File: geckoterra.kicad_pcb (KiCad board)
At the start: 2 copper layers, 50 x 50 mm, 21 parts, among them J1 Conn_WallSocket_Earth, J6 Conn_01x02, J7 Conn_01x02, J8 Conn_01x02, K1 SANYOU_SRD_Form_A, P1 Conn_WallPlug_Earth, Q1 2N3904, Q2 Q_NMOS_GDS, U1 PC817, U2 4N25

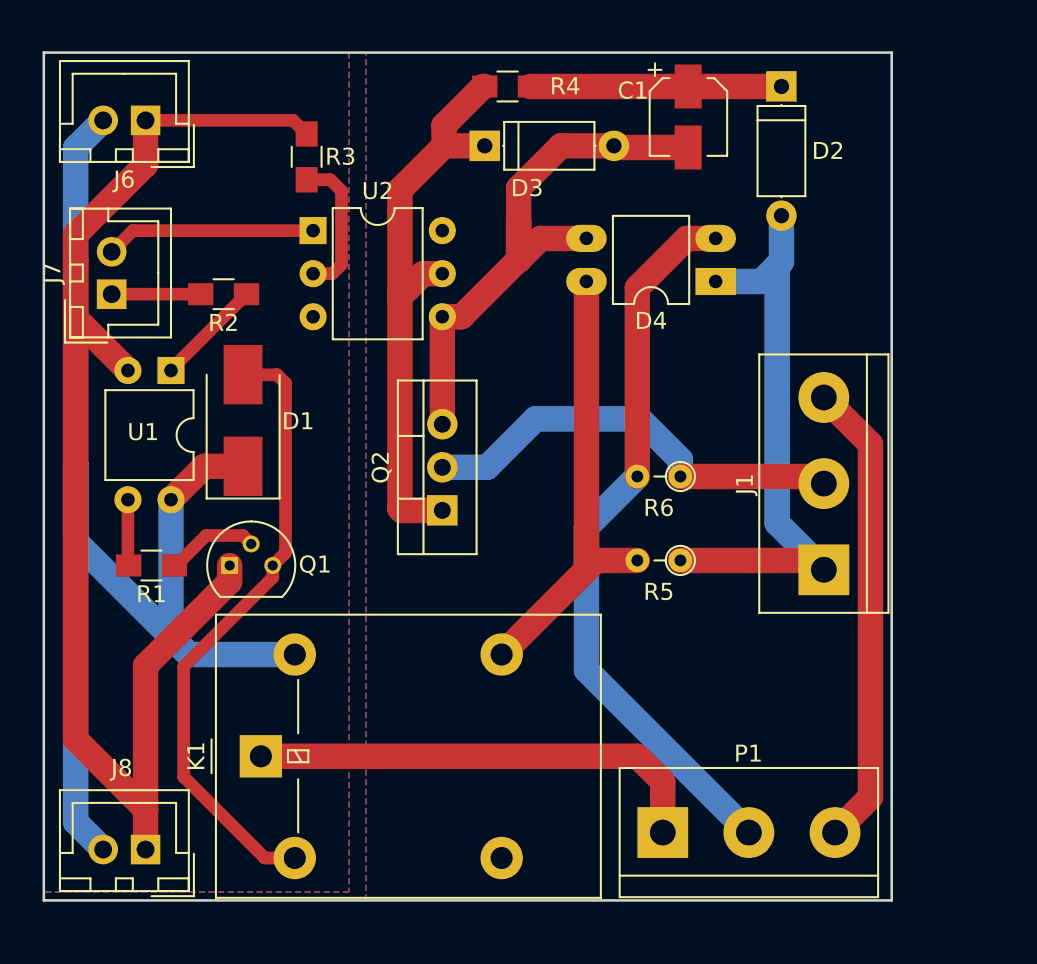
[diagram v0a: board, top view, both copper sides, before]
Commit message: Added screw holes
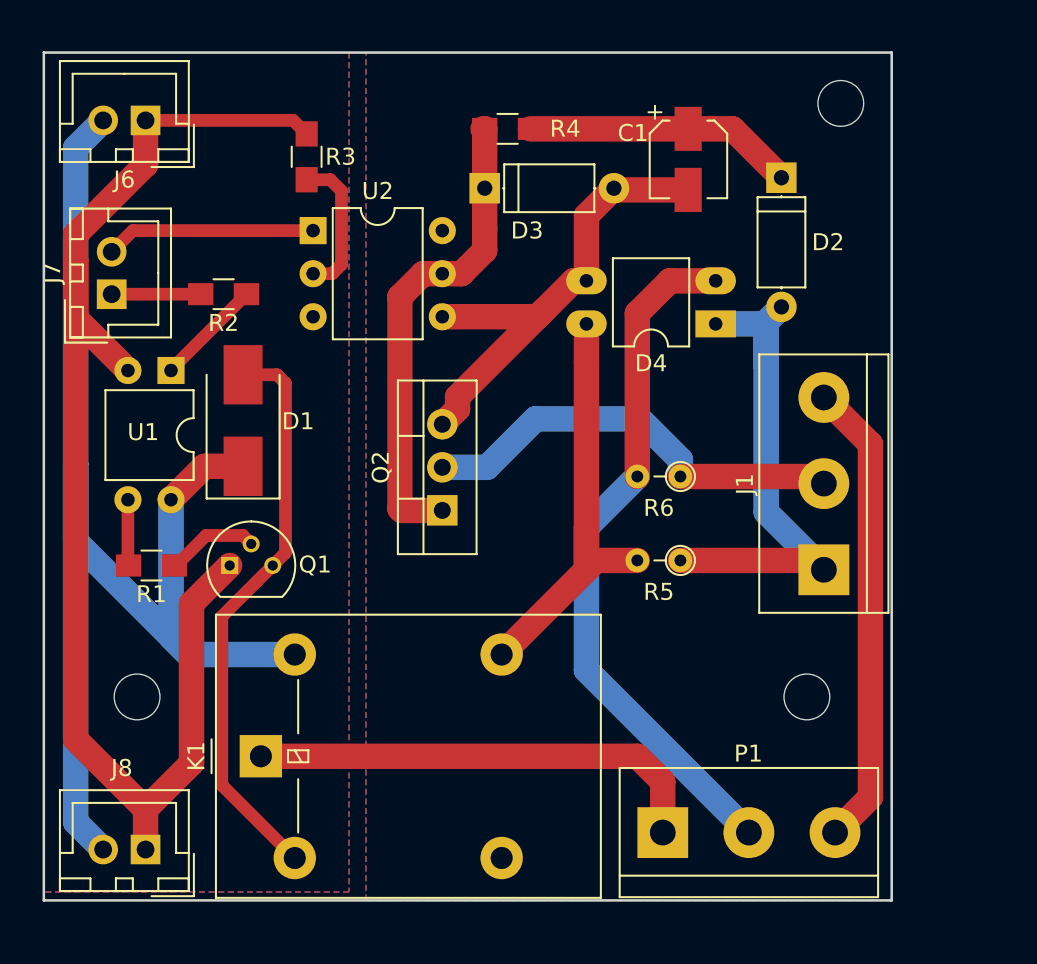
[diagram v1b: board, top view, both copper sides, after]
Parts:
- added SC1: MountingHole_2.7mm_M2.5, Mounting_Holes:MountingHole_2.7mm_M2.5, F.Cu at (55.5, 88.0)
- added SC1: MountingHole_2.7mm_M2.5, Mounting_Holes:MountingHole_2.7mm_M2.5, F.Cu at (97.0, 53.0)
- added SC2: MountingHole_2.7mm_M2.5, Mounting_Holes:MountingHole_2.7mm_M2.5, F.Cu at (95.0, 88.0)
- moved D2 5.38 mm to (93.5, 57.4)
- moved C1 2.50 mm to (88.0, 56.3)
- moved D3 2.50 mm to (76.0, 58.0)
- moved D4 2.50 mm to (89.6, 66.0)
- moved R4 2.50 mm to (77.3, 54.5)
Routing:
- net Net-(D3-Pad1): track 35.0 -> 28.4 mm
- net Net-(C1-Pad2): track 34.3 -> 29.1 mm
- net Net-(D2-Pad2): track 36.4 -> 32.5 mm
- net Net-(D1-Pad2): track 36.9 -> 34.0 mm
- net Net-(D4-Pad4): track 27.3 -> 24.8 mm
- net Net-(D4-Pad2): track 43.2 -> 41.2 mm
- net Net-(C1-Pad1): track 14.8 -> 16.0 mm

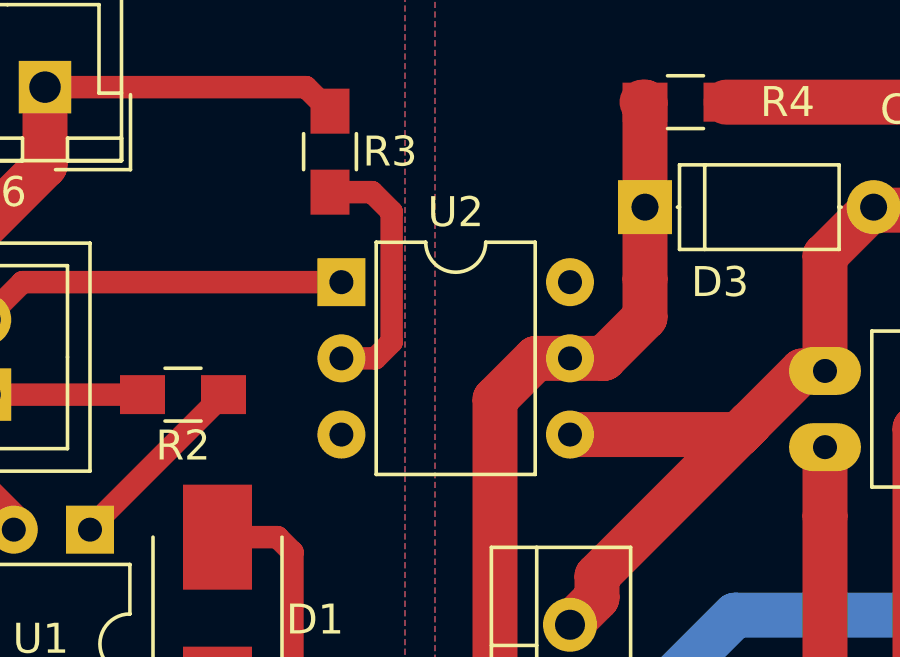
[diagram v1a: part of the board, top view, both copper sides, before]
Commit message: Add some references, change TH to SMD
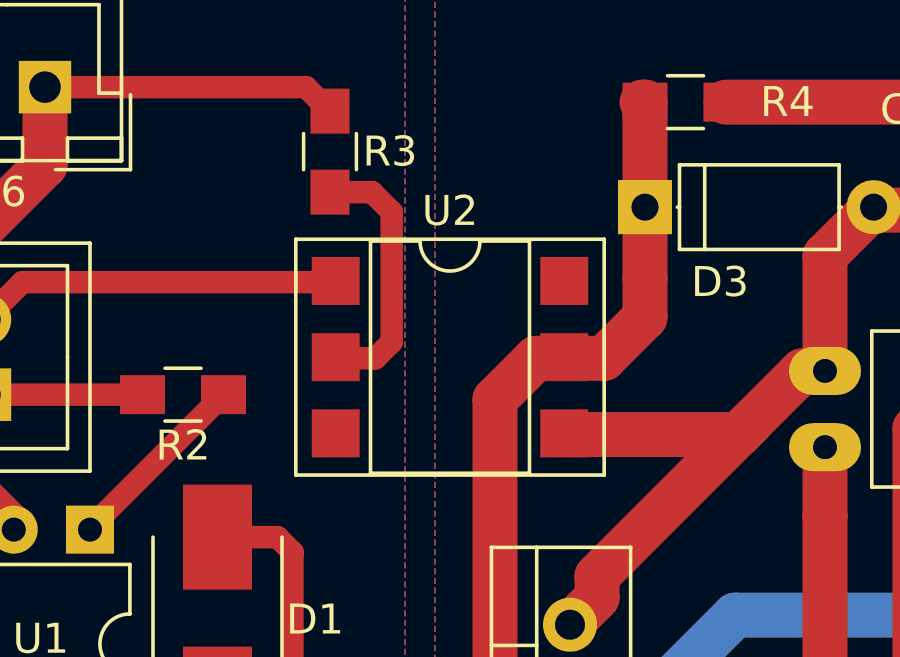
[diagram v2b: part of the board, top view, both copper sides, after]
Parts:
- U2: footprint Housings_DIP:DIP-6_W7.62mm -> Housings_DIP:DIP-6_W7.62mm_SMDSocket_SmallPads
- moved U2 4.40 mm to (69.5, 63.0)
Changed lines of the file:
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@@
-    )
-  )
-  (module Housings_DIP:DIP-6_W7.62mm (layer F.Cu)
-    (at 65.88 60.5)
-    (descr "6-lead though-hole mounted DIP package, row spacing 7.62 mm (300 mils)")
-    (tags "THT DIP DIL PDIP 2.54mm 7.62mm 300mil")
-    (fp_text reference U2 (at 3.81 -2.33) (layer F.SilkS)
-      (effects (font (size 1 1) (thickness 0.15)))
-    )
-    (fp_text value 4N25 (at 3.81 7.41) (layer F.Fab)
-      (effects (font (size 1 1) (thickness 0.15)))
-    )
-    (fp_arc (start 3.81 -1.33) (end 2.81 -1.33) (angle -180) (layer F.SilkS) (width 0.12))
-    (fp_line (start 1.635 -1.27) (end 6.985 -1.27) (layer F.Fab) (width 0.1))
-    (fp_line (start 6.985 -1.27) (end 6.985 6.35) (layer F.Fab) (width 0.1))
-    (fp_line (start 6.985 6.35) (end 0.635 6.35) (layer F.Fab) (width 0.1))
-    (fp_line (start 0.635 6.35) (end 0.635 -0.27) (layer F.Fab) (width 0.1))
-    (fp_line (start 0.635 -0.27) (end 1.635 -1.27) (layer F.Fab) (width 0.1))
-    (fp_line (start 2.81 -1.33) (end 1.16 -1.33) (layer F.SilkS) (width 0.12))
-    (fp_line (start 1.16 -1.33) (end 1.16 6.41) (layer F.SilkS) (width 0.12))
-    (fp_line (start 1.16 6.41) (end 6.46 6.41) (layer F.SilkS) (width 0.12))
-    (fp_line (start 6.46 6.41) (end 6.46 -1.33) (layer F.SilkS) (width 0.12))
-    (fp_line (start 6.46 -1.33) (end 4.81 -1.33) (layer F.SilkS) (width 0.12))
-    (fp_line (start -1.1 -1.55) (end -1.1 6.6) (layer F.CrtYd) (width 0.05))
-    (fp_line (start -1.1 6.6) (end 8.7 6.6) (layer F.CrtYd) (width 0.05))
-    (fp_line (start 8.7 6.6) (end 8.7 -1.55) (layer F.CrtYd) (width 0.05))
-    (fp_line (start 8.7 -1.55) (end -1.1 -1.55) (layer F.CrtYd) (width 0.05))
-    (fp_text user %R (at 3.81 2.54) (layer F.Fab)
-      (effects (font (size 1 1) (thickness 0.15)))
-    )
-    (pad 1 thru_hole rect (at 0 0) (size 1.6 1.6) (drill 0.8) (layers *.Cu *.Mask)
-      (net 13 /PWMPin))
-    (pad 4 thru_hole oval (at 7.62 5.08) (size 1.6 1.6) (drill 0.8) (layers *.Cu *.Mask)
-      (net 2 "Net-(C1-Pad2)"))
-    (pad 2 thru_hole oval (at 0 2.54) (size 1.6 1.6) (drill 0.8) (layers *.Cu *.Mask)
-      (net 17 "Net-(R3-Pad1)"))
-    (pad 5 thru_hole oval (at 7.62 2.54) (size 1.6 1.6) (drill 0.8) (layers *.Cu *.Mask)
-      (net 6 "Net-(D3-Pad1)"))
-    (pad 3 thru_hole oval (at 0 5.08) (size 1.6 1.6) (drill 0.8) (layers *.Cu *.Mask))
-    (pad 6 thru_hole oval (at 7.62 0) (size 1.6 1.6) (drill 0.8) (layers *.Cu *.Mask))
-    (model ${KISYS3DMOD}/Housings_DIP.3dshapes/DIP-6_W7.62mm.wrl
-      (at (xyz 0 0 0))
-      (scale (xyz 1 1 1))
-      (rotate (xyz 0 0 0))
     )
   )
@@
     (pad 1 np_thru_hole circle (at 0 0) (size 2.7 2.7) (drill 2.7) (layers *.Cu *.Mask))
   )
+  (module Housings_DIP:DIP-6_W7.62mm_SMDSocket_SmallPads (layer F.Cu)
+    (at 69.5 63)
+    (descr "6-lead though-hole mounted DIP package, row spacing 7.62 mm (300 mils), SMDSocket, SmallPads")
+    (tags "THT DIP DIL PDIP 2.54mm 7.62mm 300mil SMDSocket SmallPads")
+    (attr smd)
+    (fp_text reference U2 (at 0 -4.87) (layer F.SilkS)
+      (effects (font (size 1 1) (thickness 0.15)))
+    )
+    (fp_text value 4N25 (at 0 4.87) (layer F.Fab)
+      (effects (font (size 1 1) (thickness 0.15)))
+    )
+    (fp_arc (start 0 -3.87) (end -1 -3.87) (angle -180) (layer F.SilkS) (width 0.12))
+    (fp_line (start -2.175 -3.81) (end 3.175 -3.81) (layer F.Fab) (width 0.1))
+    (fp_line (start 3.175 -3.81) (end 3.175 3.81) (layer F.Fab) (width 0.1))
+    (fp_line (start 3.175 3.81) (end -3.175 3.81) (layer F.Fab) (width 0.1))
+    (fp_line (start -3.175 3.81) (end -3.175 -2.81) (layer F.Fab) (width 0.1))
+    (fp_line (start -3.175 -2.81) (end -2.175 -3.81) (layer F.Fab) (width 0.1))
+    (fp_line (start -5.08 -3.87) (end -5.08 3.87) (layer F.Fab) (width 0.1))
+    (fp_line (start -5.08 3.87) (end 5.08 3.87) (layer F.Fab) (width 0.1))
+    (fp_line (start 5.08 3.87) (end 5.08 -3.87) (layer F.Fab) (width 0.1))
+    (fp_line (start 5.08 -3.87) (end -5.08 -3.87) (layer F.Fab) (width 0.1))
+    (fp_line (start -1 -3.87) (end -2.65 -3.87) (layer F.SilkS) (width 0.12))
+    (fp_line (start -2.65 -3.87) (end -2.65 3.87) (layer F.SilkS) (width 0.12))
+    (fp_line (start -2.65 3.87) (end 2.65 3.87) (layer F.SilkS) (width 0.12))
+    (fp_line (start 2.65 3.87) (end 2.65 -3.87) (layer F.SilkS) (width 0.12))
+    (fp_line (start 2.65 -3.87) (end 1 -3.87) (layer F.SilkS) (width 0.12))
+    (fp_line (start -5.14 -3.93) (end -5.14 3.93) (layer F.SilkS) (width 0.12))
+    (fp_line (start -5.14 3.93) (end 5.14 3.93) (layer F.SilkS) (width 0.12))
+    (fp_line (start 5.14 3.93) (end 5.14 -3.93) (layer F.SilkS) (width 0.12))
+    (fp_line (start 5.14 -3.93) (end -5.14 -3.93) (layer F.SilkS) (width 0.12))
+    (fp_line (start -5.35 -4.15) (end -5.35 4.15) (layer F.CrtYd) (width 0.05))
+    (fp_line (start -5.35 4.15) (end 5.35 4.15) (layer F.CrtYd) (width 0.05))
+    (fp_line (start 5.35 4.15) (end 5.35 -4.15) (layer F.CrtYd) (width 0.05))
+    (fp_line (start 5.35 -4.15) (end -5.35 -4.15) (layer F.CrtYd) (width 0.05))
+    (fp_text user %R (at 0 0) (layer F.Fab)
+      (effects (font (size 1 1) (thickness 0.15)))
+    )
+    (pad 1 smd rect (at -3.81 -2.54) (size 1.6 1.6) (layers F.Cu F.Paste F.Mask)
+      (net 13 /PWMPin))
+    (pad 4 smd rect (at 3.81 2.54) (size 1.6 1.6) (layers F.Cu F.Paste F.Mask)
+      (net 2 "Net-(C1-Pad2)"))
+    (pad 2 smd rect (at -3.81 0) (size 1.6 1.6) (layers F.Cu F.Paste F.Mask)
+      (net 17 "Net-(R3-Pad1)"))
+    (pad 5 smd rect (at 3.81 0) (size 1.6 1.6) (layers F.Cu F.Paste F.Mask)
+      (net 6 "Net-(D3-Pad1)"))
+    (pad 3 smd rect (at -3.81 2.54) (size 1.6 1.6) (layers F.Cu F.Paste F.Mask))
+    (pad 6 smd rect (at 3.81 -2.54) (size 1.6 1.6) (layers F.Cu F.Paste F.Mask))
+    (model ${KISYS3DMOD}/Housings_DIP.3dshapes/DIP-6_W7.62mm_SMDSocket.wrl
+      (at (xyz 0 0 0))
+      (scale (xyz 1 1 1))
+      (rotate (xyz 0 0 0))
+    )
+  )
   (gr_line (start 50 100) (end 50 50) (layer Edge.Cuts) (width 0.15))

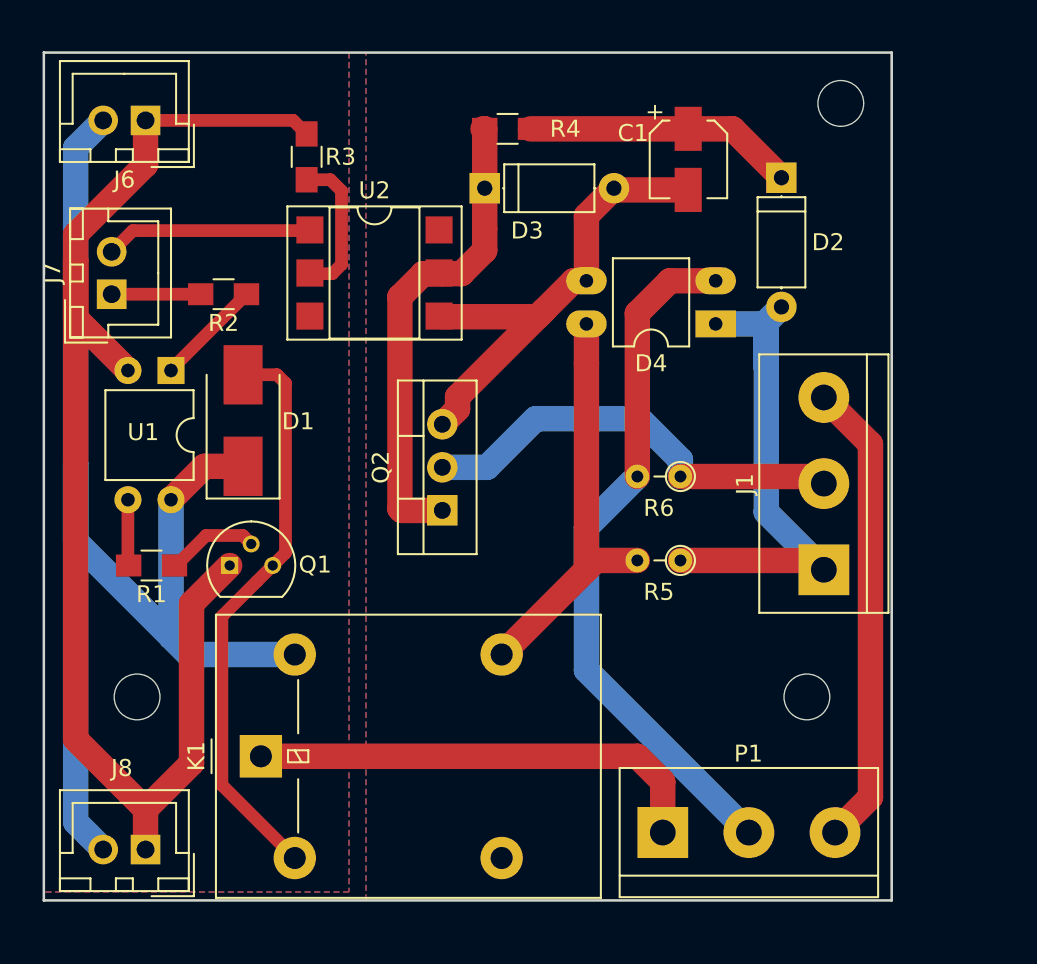
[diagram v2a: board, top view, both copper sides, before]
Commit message: Add urls. Add correct footprints. Change PCB to add the big capa.
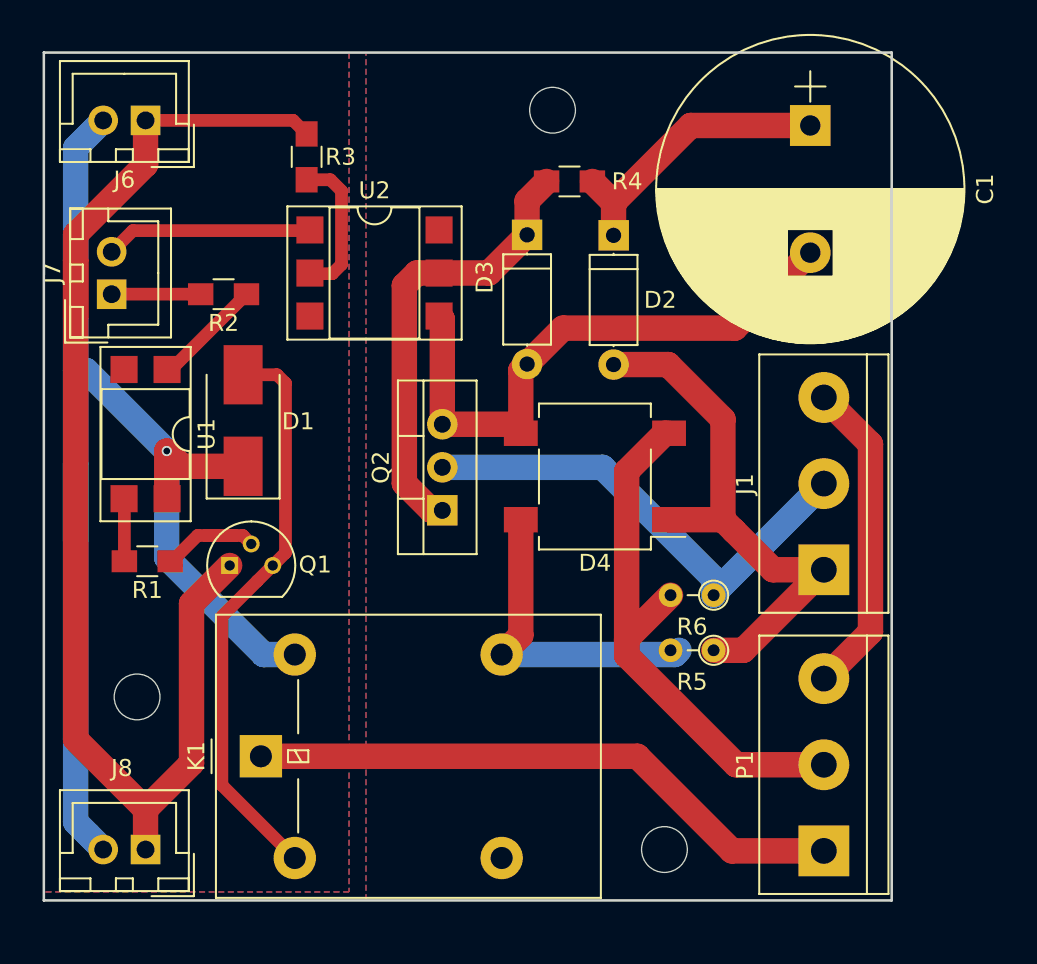
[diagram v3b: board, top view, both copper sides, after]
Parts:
- C1: footprint Capacitors_SMD:CP_Elec_4x4.5 -> Capacitors_THT:CP_Radial_D18.0mm_P7.50mm
- D4: footprint Housings_DIP:DIP-4_W7.62mm_LongPads -> Diodes_SMD:Diode_Bridge_DFS
- U1: footprint Housings_DIP:DIP-4_W7.62mm -> Housings_DIP:DIP-4_W7.62mm_SMDSocket_SmallPads
- moved SC1 17.0 mm to (80.0, 53.4)
- moved SC2 12.3 mm to (86.6, 97.0)
- moved D4 11.5 mm to (82.5, 75.0)
- moved D2 10.5 mm to (83.6, 60.8)
- moved P1 9.56 mm to (96.0, 97.1), turned to 90 degrees
- moved C1 7.47 mm to (95.2, 54.3)
- moved R6 7.27 mm to (89.5, 82.0)
- moved R5 5.65 mm to (89.5, 85.2)
- moved R4 4.79 mm to (81.0, 57.6)
- moved U1 4.04 mm to (56.0, 72.5)
- moved D3 3.72 mm to (78.5, 60.8), turned to 270 degrees
- moved R1 0.35 mm to (56.1, 80.0)
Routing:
- net Net-(J1-Pad3): track 27.7 -> 18.9 mm
- net Net-(K1-Pad1): track 27.3 -> 35.5 mm
- net Net-(D4-Pad2): track 41.2 -> 33.2 mm
- net Net-(C1-Pad2): track 29.1 -> 35.0 mm
- net Net-(D4-Pad4): track 24.8 -> 19.0 mm
- net GND: track 80.5 -> 76.1 mm
- net Net-(J1-Pad2): track 26.4 -> 30.2 mm
- net Net-(Q1-Pad2): track 5.47 -> 7.40 mm
- net Net-(D3-Pad1): track 28.4 -> 26.8 mm
- net Net-(D2-Pad2): track 32.5 -> 34.1 mm
- net Net-(C1-Pad1): track 16.0 -> 17.2 mm
- net +5V: track 79.2 -> 80.2 mm, vias 0 -> 1

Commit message: Ending fixes (smaller capa footprint). Sent to seeed.
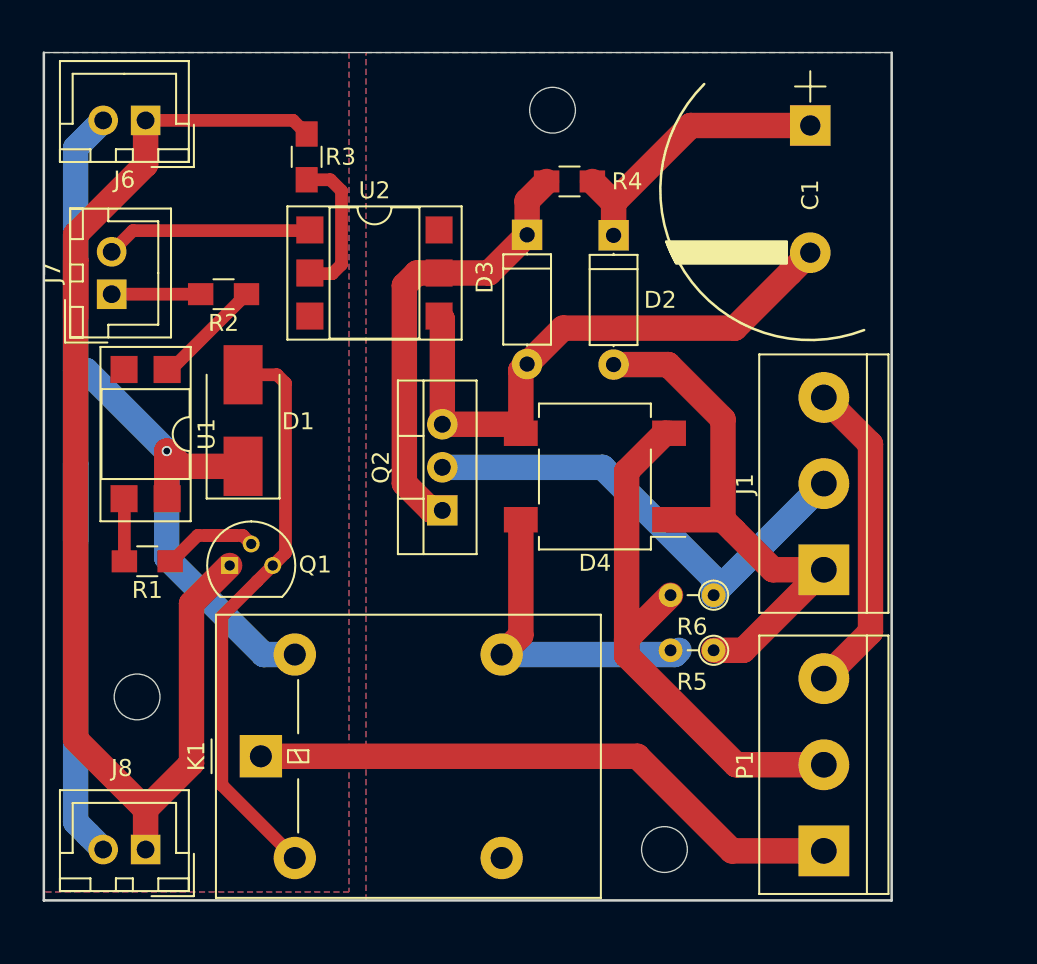
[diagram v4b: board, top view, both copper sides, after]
